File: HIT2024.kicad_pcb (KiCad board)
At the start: 2 copper layers, 24 x 50 mm, 3 parts

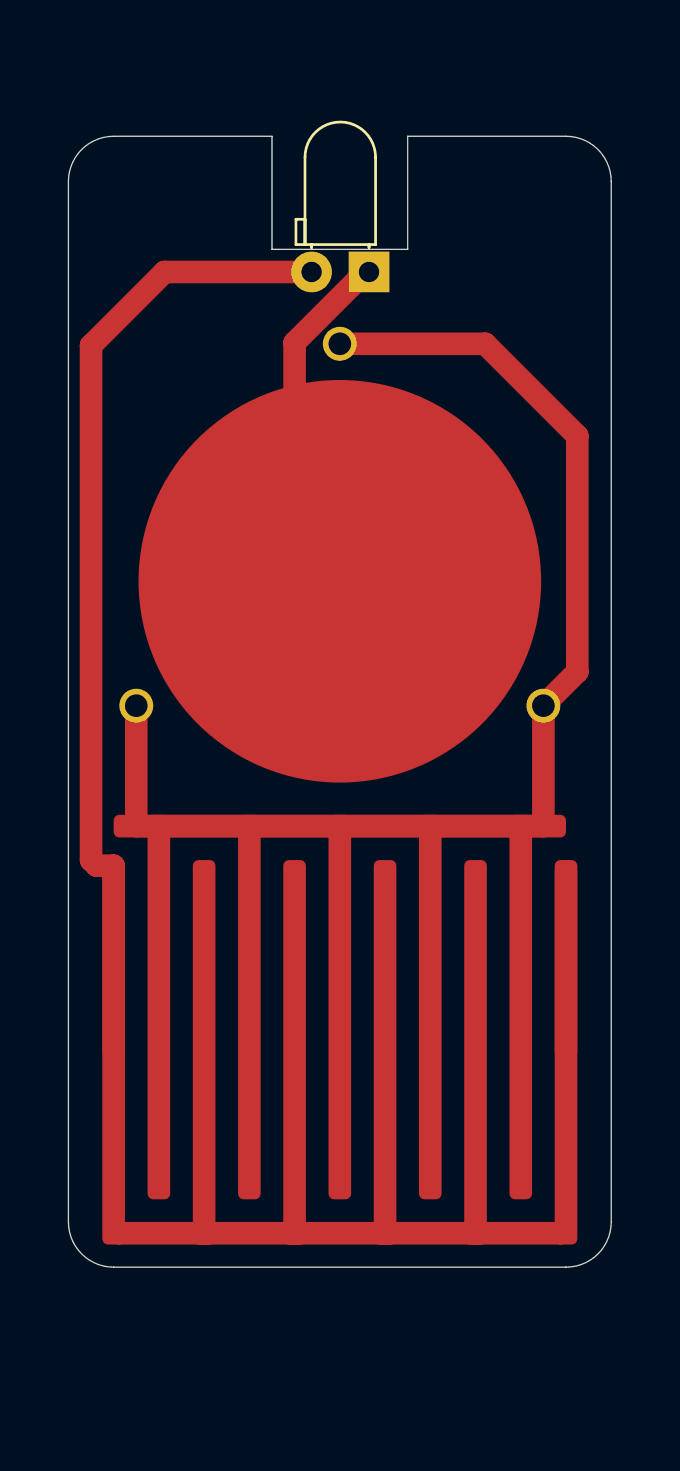
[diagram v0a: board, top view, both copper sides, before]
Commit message: bigger pads, updated battery mounting, 0,6mm holes, finer touch sensor, bigger led hole, +- marking
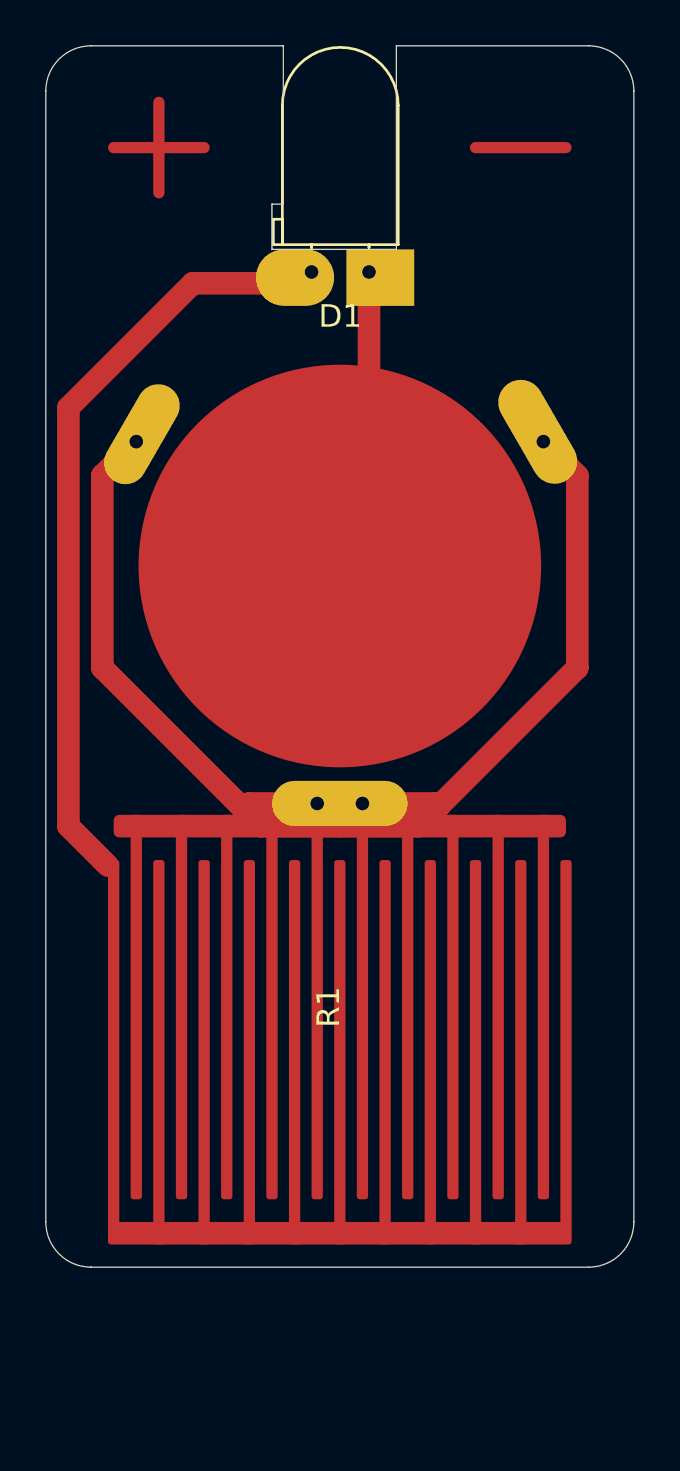
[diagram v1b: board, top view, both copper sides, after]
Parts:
- D1: footprint LED_THT:LED_D3.0mm_Horizontal_O1.27mm_Z2.0mm -> LED_THT:LED_D5.0mm_Horizontal_O1.27mm_Z3.0mm
- R1: footprint CHAIR:Humidity_Sensor_Printed_Electronics -> CHAIR:Humidity_Sensor_Printed_Electronics_Fine
- moved BT1 0.67 mm to (71.0, 36.0), turned to 0 degrees
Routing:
- net Net-(D1-A): track 51.2 -> 34.2 mm
- net Net-(BT1--): track 21.1 -> 13.5 mm
- net Net-(BT1-+): track 53.4 -> 54.8 mm
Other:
- board size 24 x 50 mm -> 26 x 54 mm

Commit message: adds slots for velostat
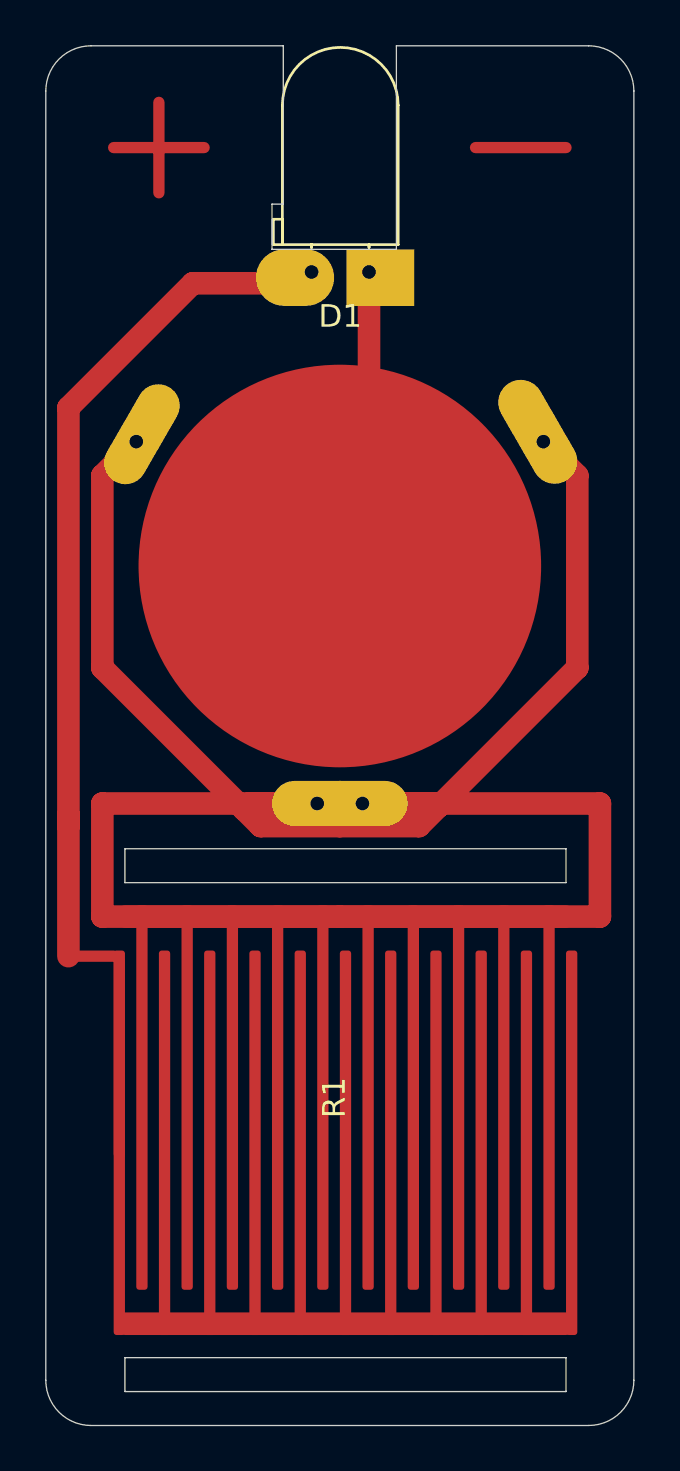
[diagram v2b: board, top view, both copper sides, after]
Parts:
- moved R1 4.01 mm to (71.2, 59.5)
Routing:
- net Net-(BT1-+): track 54.8 -> 106.8 mm
- net Net-(D1-A): track 34.2 -> 48.5 mm
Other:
- board size 26 x 54 mm -> 26 x 61 mm
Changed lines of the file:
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@@
 	(footprint "CHAIR:Humidity_Sensor_Printed_Electronics_Fine"
 		(layer "F.Cu")
-		(at 71 55.5 90)
+		(at 71.25 59.5 90)
 		(descr "PCB Footprint")
 		(property "Reference" "R1"
@@
 	)
 	(gr_arc
-		(start 84 65)
-		(mid 83.414214 66.414214)
-		(end 82 67)
+		(start 84 72)
+		(mid 83.414214 73.414214)
+		(end 82 74)
 		(stroke
 			(width 0.05)
@@
 	)
 	(gr_line
-		(start 84 65)
+		(start 84 72)
 		(end 84 15)
 		(stroke
@@
 		(layer "Edge.Cuts")
 	)
+	(gr_rect
+		(start 61.5 48.5)
+		(end 81 50)
+		(stroke
+			(width 0.05)
+			(type default)
+		)
+		(fill none)
+		(layer "Edge.Cuts")
+	)
 	(gr_line
 		(start 60 13)
@@
 			(type default)
 		)
+		(layer "Edge.Cuts")
+	)
+	(gr_rect
+		(start 61.5 71)
+		(end 81 72.5)
+		(stroke
+			(width 0.05)
+			(type default)
+		)
+		(fill none)
 		(layer "Edge.Cuts")
 	)
@@
 	)
 	(gr_line
-		(start 60 67)
-		(end 82 67)
+		(start 60 74)
+		(end 82 74)
 		(stroke
 			(width 0.05)
@@
 	(gr_line
 		(start 58 15)
-		(end 58 65)
+		(end 58 72)
 		(stroke
 			(width 0.05)
@@
 	)
 	(gr_arc
-		(start 60 67)
-		(mid 58.585786 66.414214)
-		(end 58 65)
+		(start 60 74)
+		(mid 58.585786 73.414214)
+		(end 58 72)
 		(stroke
 			(width 0.05)
@@
 	)
 	(segment
+		(start 82.5 46.5)
+		(end 72 46.5)
+		(width 1)
+		(layer "F.Cu")
+		(net 1)
+	)
+	(segment
 		(start 75.25 46.5)
 		(end 75.375 46.625)
@@
 	)
 	(segment
+		(start 60.5 51.5)
+		(end 60.5 46.5)
+		(width 1)
+		(layer "F.Cu")
+		(net 1)
+	)
+	(segment
+		(start 82.5 51.5)
+		(end 82.5 46.5)
+		(width 1)
+		(layer "F.Cu")
+		(net 1)
+	)
+	(segment
 		(start 81.5 32)
 		(end 80 30.5)
@@
 	)
 	(segment
+		(start 60.5 46.5)
+		(end 70 46.5)
+		(width 1)
+		(layer "F.Cu")
+		(net 1)
+	)
+	(segment
 		(start 81.5 40.5)
 		(end 81.5 32)
@@
 	)
 	(segment
+		(start 60.5 51.5)
+		(end 71 51.5)
+		(width 1)
+		(layer "F.Cu")
+		(net 1)
+	)
+	(segment
 		(start 67.5 47.5)
 		(end 71 47.5)
@@
 	)
 	(segment
+		(start 71 51.5)
+		(end 82.5 51.5)
+		(width 1)
+		(layer "F.Cu")
+		(net 1)
+	)
+	(segment
 		(start 62 30.5)
 		(end 60.5 32)
@@
 	)
 	(segment
+		(start 59 47)
+		(end 59 47.5)
+		(width 1)
+		(layer "F.Cu")
+		(net 3)
+	)
+	(segment
+		(start 59 47)
+		(end 59 53.25)
+		(width 1)
+		(layer "F.Cu")
+		(net 3)
+	)
+	(segment
+		(start 61.25 53.5)
+		(end 61.25 62)
+		(width 0.5)
+		(layer "F.Cu")
+		(net 3)
+	)
+	(segment
+		(start 59 29)
+		(end 59 47)
+		(width 1)
+		(layer "F.Cu")
+		(net 3)
+	)
+	(segment
+		(start 59 53.25)
+		(end 61 53.25)
+		(width 0.5)
+		(layer "F.Cu")
+		(net 3)
+	)
+	(segment
 		(start 64.5 23.5)
 		(end 59 29)
@@
 	)
 	(segment
-		(start 59 47.5)
-		(end 60.75 49.25)
-		(width 1)
-		(layer "F.Cu")
-		(net 3)
-	)
-	(segment
 		(start 69.75 23)
 		(end 69.25 23.5)
@@
 		(net 3)
 	)
-	(segment
-		(start 59 29)
-		(end 59 47.5)
-		(width 1)
-		(layer "F.Cu")
-		(net 3)
-	)
 	(zone
 		(net 1)
@@
 		(name "$teardrop_padvia$")
 		(hatch full 0.1)
-		(priority 30006)
+		(priority 30002)
 		(attr
 			(teardrop
@@
 		(polygon
 			(pts
-				(xy 70 47) (xy 70 48) (xy 72.259015 47.488979) (xy 72.001 46.5) (xy 70.019215 46.372474)
+				(xy 67.019215 46) (xy 67.019215 47) (xy 68.80491 47.480785) (xy 70.001 46.5) (xy 68.80491 45.519215)
 			)
 		)
@@
 		(name "$teardrop_padvia$")
 		(hatch full 0.1)
-		(priority 30001)
+		(priority 30003)
 		(attr
 			(teardrop
@@
 	)
 	(zone
-		(net 3)
-		(net_name "Net-(D1-A)")
+		(net 1)
+		(net_name "Net-(BT1-+)")
 		(layer "F.Cu")
 		(name "$teardrop_padvia$")
 		(hatch full 0.1)
-		(priority 30000)
+		(priority 30007)
 		(attr
 			(teardrop
@@
 		(polygon
 			(pts
-				(xy 66.323963 23) (xy 66.323963 24) (xy 67.857307 24.286874) (xy 69.751 23) (xy 67.757025 22.28033)
+				(xy 60 32.718431) (xy 61 32.718431) (xy 61.936395 32.287467) (xy 62 30.499) (xy 60.62034 31.131043)
 			)
 		)
@@
 		(name "$teardrop_padvia$")
 		(hatch full 0.1)
-		(priority 30003)
+		(priority 30009)
 		(attr
 			(teardrop
@@
 		(polygon
 			(pts
-				(xy 81 32.79978) (xy 82 32.79978) (xy 81.44693 31.044586) (xy 80 30.499) (xy 80.057711 32.262898)
+				(xy 70 47) (xy 70 48) (xy 72.259015 47.488979) (xy 72.001 46.5) (xy 70.019215 46.372474)
 			)
 		)
@@
 		(name "$teardrop_padvia$")
 		(hatch full 0.1)
-		(priority 30005)
+		(priority 30010)
 		(attr
 			(teardrop
@@
 		(polygon
 			(pts
-				(xy 60 32.718431) (xy 61 32.718431) (xy 61.936395 32.287467) (xy 62 30.499) (xy 60.62034 31.131043)
+				(xy 70 47) (xy 70 48) (xy 72.259015 47.488979) (xy 72.001 46.5) (xy 70.019215 46.372474)
 			)
 		)
 	)
 	(zone
-		(net 1)
-		(net_name "Net-(BT1-+)")
+		(net 3)
+		(net_name "Net-(D1-A)")
 		(layer "F.Cu")
 		(name "$teardrop_padvia$")
 		(hatch full 0.1)
-		(priority 30002)
+		(priority 30000)
 		(attr
 			(teardrop
@@
 		(polygon
 			(pts
-				(xy 67.019215 46) (xy 67.019215 47) (xy 68.80491 47.480785) (xy 70.001 46.5) (xy 68.80491 45.519215)
+				(xy 66.323963 23) (xy 66.323963 24) (xy 67.857307 24.286874) (xy 69.751 23) (xy 67.757025 22.28033)
 			)
 		)
 	)
 	(zone
-		(net 1)
-		(net_name "Net-(BT1-+)")
+		(net 2)
+		(net_name "Net-(BT1--)")
 		(layer "F.Cu")
 		(name "$teardrop_padvia$")
 		(hatch full 0.1)
-		(priority 30007)
+		(priority 30006)
 		(attr
 			(teardrop
@@
 		(polygon
 			(pts
-				(xy 68 47) (xy 68 48) (xy 70.259015 47.488979) (xy 70.001 46.5) (xy 68.019215 46.372474)
+				(xy 71.79 25.5) (xy 72.79 25.5) (xy 73.29 24.5) (xy 72.29 22.999) (xy 71.29 24.5)
 			)
 		)
 	)
 	(zone
-		(net 2)
-		(net_name "Net-(BT1--)")
-		(layer "F.Cu")
-		(name "$teardrop_padvia$")
+		(net 3)
+		(net_name "Net-(D1-A)")
+		(layer "F.Cu")
+		(name "$teardrop_track$")
 		(hatch full 0.1)
-		(priority 30004)
+		(priority 30011)
 		(attr
 			(teardrop
-				(type padvia)
+				(type track_end)
 			)
 		)
@@
 		(polygon
 			(pts
-				(xy 71.79 25.5) (xy 72.79 25.5) (xy 73.29 24.5) (xy 72.29 22.999) (xy 71.29 24.5)
+				(xy 60 53.5) (xy 60 53) (xy 59.191342 52.78806) (xy 58.999 53.25) (xy 59.191342 53.71194)
 			)
 		)
@@
 		(name "$teardrop_padvia$")
 		(hatch full 0.1)
-		(priority 30008)
+		(priority 30001)
 		(attr
 			(teardrop
@@
 		(polygon
 			(pts
-				(xy 70 47) (xy 70 48) (xy 72.259015 47.488979) (xy 72.001 46.5) (xy 70.019215 46.372474)
-			)
-		)
+				(xy 74.980785 47) (xy 74.980785 46) (xy 73.19509 45.519215) (xy 71.999 46.5) (xy 73.19509 47.480785)
+			)
+		)
+	)
+	(zone
+		(net 1)
+		(net_name "Net-(BT1-+)")
+		(layer "F.Cu")
+		(name "$teardrop_padvia$")
+		(hatch full 0.1)
+		(priority 30008)
+		(attr
+			(teardrop
+				(type padvia)
+			)
+		)
+		(connect_pads yes
+			(clearance 0)
+		)
+		(min_thickness 0.0254)
+		(filled_areas_thickness no)
+		(fill yes
+			(thermal_gap 0.5)
+			(thermal_bridge_width 0.5)
+			(island_removal_mode 1)
+			(island_area_min 10)
+		)
+		(polygon
+			(pts
+				(xy 68 47) (xy 68 48) (xy 70.259015 47.488979) (xy 70.001 46.5) (xy 68.019215 46.372474)
+			)
+		)
+	)
+	(zone
+		(net 1)
+		(net_name "Net-(BT1-+)")
+		(layer "F.Cu")
+		(name "$teardrop_padvia$")
+		(hatch full 0.1)
+		(priority 30005)
+		(attr
+			(teardrop
+				(type padvia)
+			)
+		)
+		(connect_pads yes
+			(clearance 0)
+		)
+		(min_thickness 0.0254)
+		(filled_areas_thickness no)
+		(fill yes
+			(thermal_gap 0.5)
+			(thermal_bridge_width 0.5)
+			(island_removal_mode 1)
+			(island_area_min 10)
+		)
+		(polygon
+			(pts
+				(xy 81 32.79978) (xy 82 32.79978) (xy 81.44693 31.044586) (xy 80 30.499) (xy 80.057711 32.262898)
+			)
+		)
+	)
+	(zone
+		(net 1)
+		(net_name "Net-(BT1-+)")
+		(layer "F.Cu")
+		(name "$teardrop_padvia$")
+		(hatch full 0.1)
+		(priority 30004)
+		(attr
+			(teardrop
+				(type padvia)
+			)
+		)
+		(connect_pads yes
+			(clearance 0)
+		)
+		(min_thickness 0.0254)
+		(filled_areas_thickness no)
+		(fill yes
+			(thermal_gap 0.5)
+			(thermal_bridge_width 0.5)
+			(island_removal_mode 1)
+			(island_area_min 10)
+		)
+		(polygon
+			(pts
+				(xy 67.019215 46) (xy 67.019215 47) (xy 68.80491 47.480785) (xy 70.001 46.5) (xy 68.80491 45.519215)
+			)
+		)
